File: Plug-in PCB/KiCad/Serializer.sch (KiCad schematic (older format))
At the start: 32 parts, among them J8 Conn_Coaxial, U1 DS90UB933-Q1

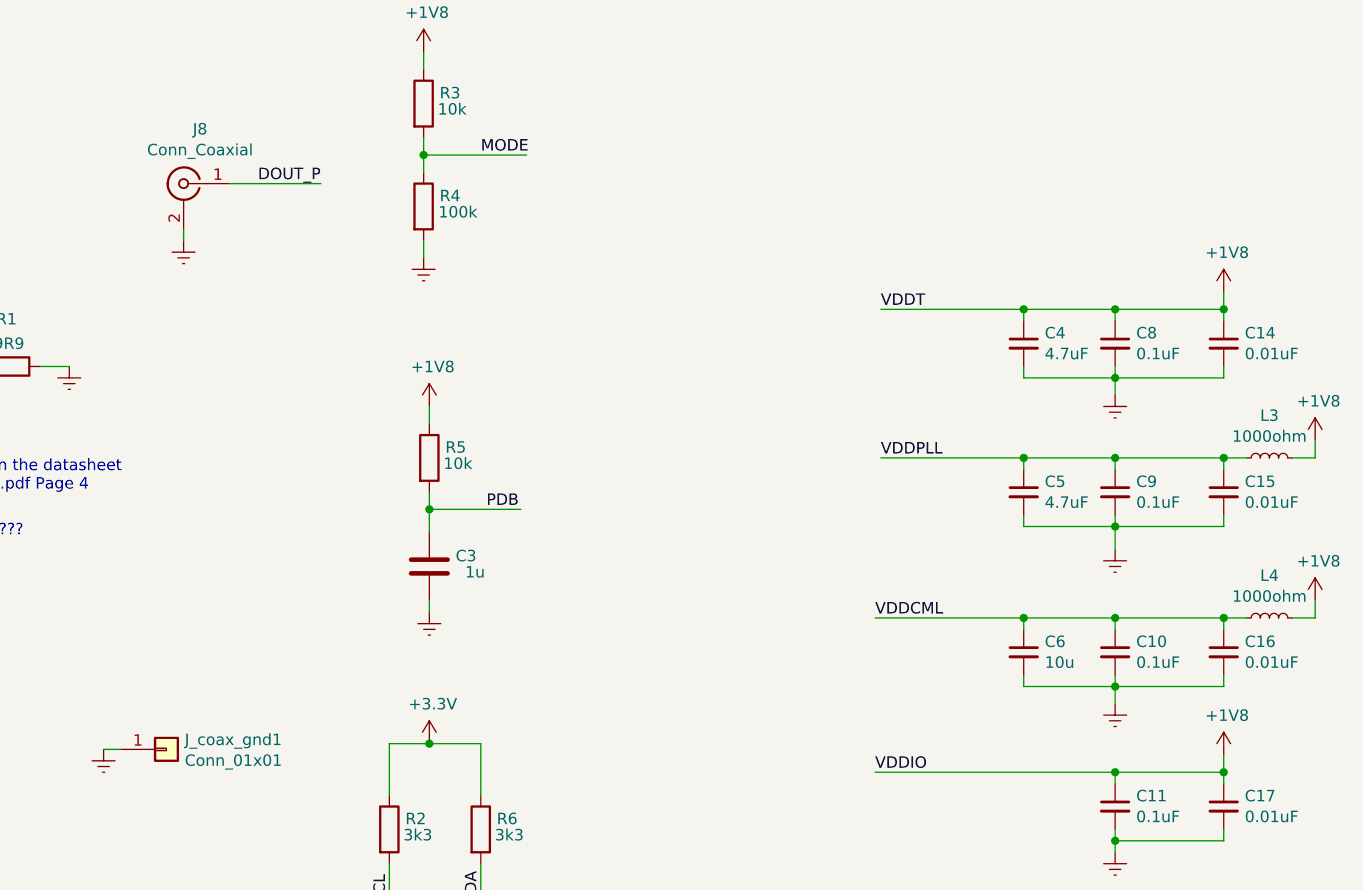
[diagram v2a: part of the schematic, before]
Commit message: Change MCU and Serializer Power to 3.3V
1. MCU VDDIO, SWD, VDDIN, VDDUTMII powered at 3.3V

2. Serializer VDDIO, PDB powered at 3.3V

3. Layout changed (Pins enlarged, Coax_Gnd added, Coax connector moved closer to seralizer)
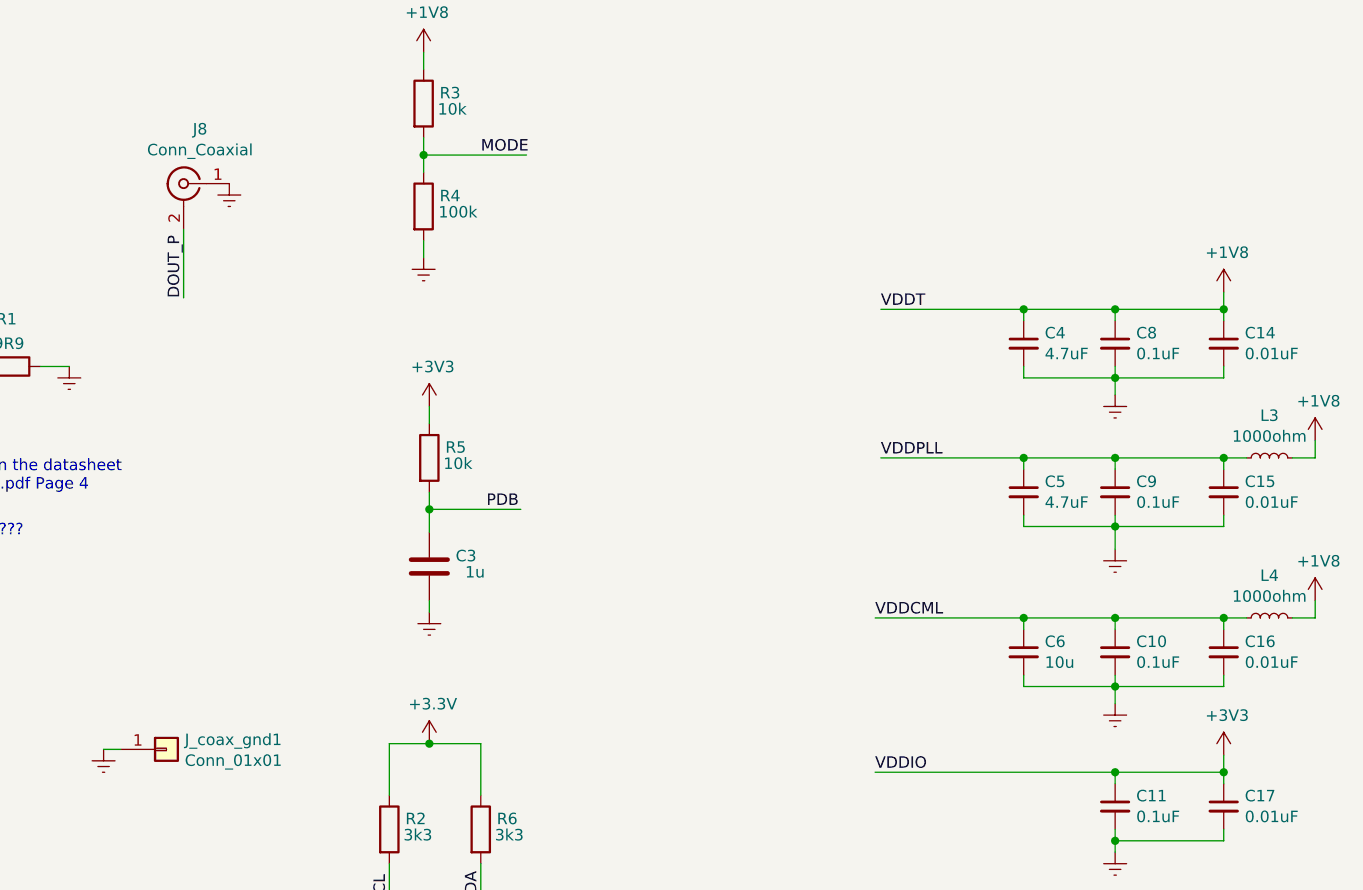
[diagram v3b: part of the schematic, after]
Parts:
- J_coax_gnd1: footprint .Connector:Conn_1x1_700_Circular_Pad -> .Connector:Conn_1x1_100x100_Pad
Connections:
- net labels added: +3V3
- wire segments 121 -> 120
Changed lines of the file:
@@
 Wire Wire Line
 	9775 5225 9775 5175
-$Comp
-L power:+1V8 #PWR0118
-U 1 1 5CD64A59
-P 10250 4800
-F 0 "#PWR0118" H 10250 4650 50  0001 C CNN
-F 1 "+1V8" H 10265 4973 50  0000 C CNN
-F 2 "" H 10250 4800 50  0001 C CNN
-F 3 "" H 10250 4800 50  0001 C CNN
-	1    10250 4800
-	1    0    0    -1
-$EndComp
 Wire Wire Line
 	10250 4800 10250 4875
@@
 Wire Wire Line
 	6750 2175 6750 2250
-$Comp
-L power:+1V8 #PWR0121
-U 1 1 5CDF8F09
-P 6775 3275
-F 0 "#PWR0121" H 6775 3125 50  0001 C CNN
-F 1 "+1V8" H 6790 3448 50  0000 C CNN
-F 2 "" H 6775 3275 50  0001 C CNN
-F 3 "" H 6775 3275 50  0001 C CNN
-	1    6775 3275
-	1    0    0    -1
-$EndComp
 $Comp
 L Device:R R5
@@
 	0    1    1    0
 $EndComp
-Wire Wire Line
-	5700 2500 5700 2550
 $Comp
 L .Connector:Conn_01x01 J_coax_gnd1
@@
 F 0 "J_coax_gnd1" H 5705 4817 50  0000 L CNN
 F 1 "Conn_01x01" H 5705 4726 50  0000 L CNN
-F 2 ".Connector:Conn_1x1_700_Circular_Pad" H 5625 4775 50  0001 C CNN
+F 2 ".Connector:Conn_1x1_100x100_Pad" H 5625 4775 50  0001 C CNN
 F 3 "~" H 5625 4775 50  0001 C CNN
 	1    5625 4775
@@
 Wire Wire Line
 	4250 2250 4250 2600
-Text Label 6025 2300 0    50   ~ 0
+Text Label 5700 2800 1    50   ~ 0
 DOUT_P
-Wire Wire Line
-	5900 2300 6300 2300
 Text Label 7875 950  0    50   ~ 0
 DOUT_P
@@
 $EndComp
 $Comp
-L power:Earth #PWR0106
-U 1 1 5D5F562A
-P 5700 2550
-F 0 "#PWR0106" H 5700 2300 50  0001 C CNN
-F 1 "Earth" H 5700 2400 50  0001 C CNN
-F 2 "" H 5700 2550 50  0001 C CNN
-F 3 "~" H 5700 2550 50  0001 C CNN
-	1    5700 2550
-	1    0    0    -1
-$EndComp
-$Comp
 L power:Earth #PWR0107
 U 1 1 5D5F5B07
@@
 	1    0    0    -1
 $EndComp
+Wire Wire Line
+	5700 2800 5700 2500
 Wire Bus Line
 	1450 3250 1450 3600
 Wire Bus Line
 	1450 3600 1450 3950
+$Comp
+L power:Earth #PWR0106
+U 1 1 5D67C474
+P 5900 2300
+F 0 "#PWR0106" H 5900 2050 50  0001 C CNN
+F 1 "Earth" H 5900 2150 50  0001 C CNN
+F 2 "" H 5900 2300 50  0001 C CNN
+F 3 "~" H 5900 2300 50  0001 C CNN
+	1    5900 2300
+	1    0    0    -1
+$EndComp
+$Comp
+L power:+3V3 #PWR?
+U 1 1 5D6CA288
+P 10250 4800
+F 0 "#PWR?" H 10250 4650 50  0001 C CNN
+F 1 "+3V3" H 10265 4973 50  0000 C CNN
+F 2 "" H 10250 4800 50  0001 C CNN
+F 3 "" H 10250 4800 50  0001 C CNN
+	1    10250 4800
+	1    0    0    -1
+$EndComp
+$Comp
+L power:+3V3 #PWR?
+U 1 1 5D6CA936
+P 6775 3275
+F 0 "#PWR?" H 6775 3125 50  0001 C CNN
+F 1 "+3V3" H 6790 3448 50  0000 C CNN
+F 2 "" H 6775 3275 50  0001 C CNN
+F 3 "" H 6775 3275 50  0001 C CNN
+	1    6775 3275
+	1    0    0    -1
+$EndComp
 $EndSCHEMATC
